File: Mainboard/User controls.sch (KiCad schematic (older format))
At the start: 7 parts, among them J2 JST-PH 01x10, J5 JST-PH 01x02, J6 JST-PH 01x02

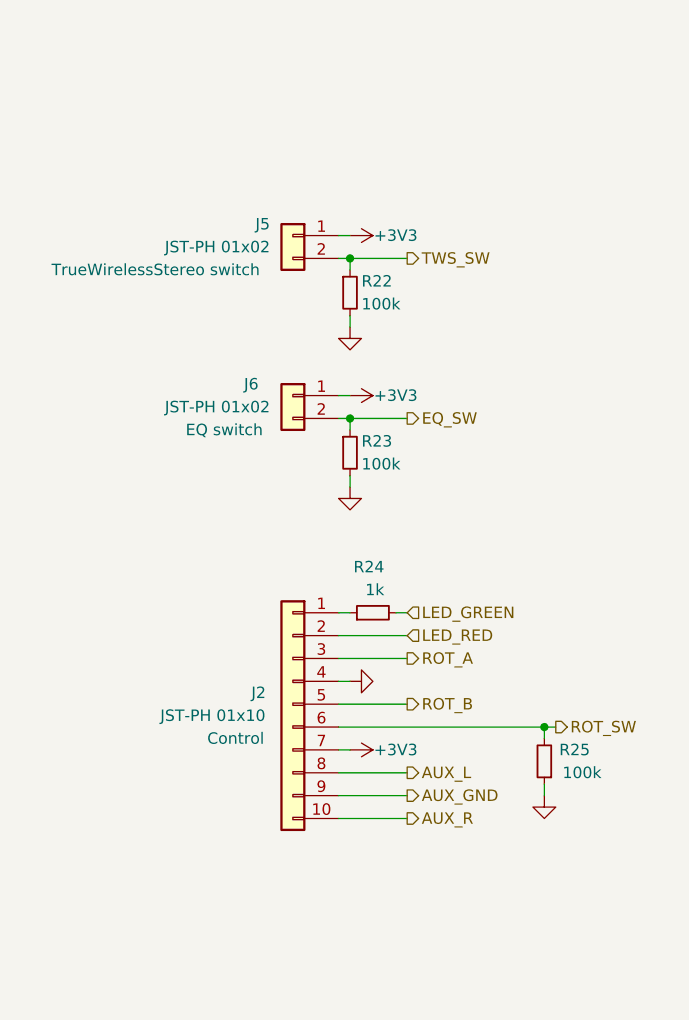
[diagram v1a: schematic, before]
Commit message: Before testing CH340B and VCHG
Cleaned up amp lay-out a bit in the meanwhile
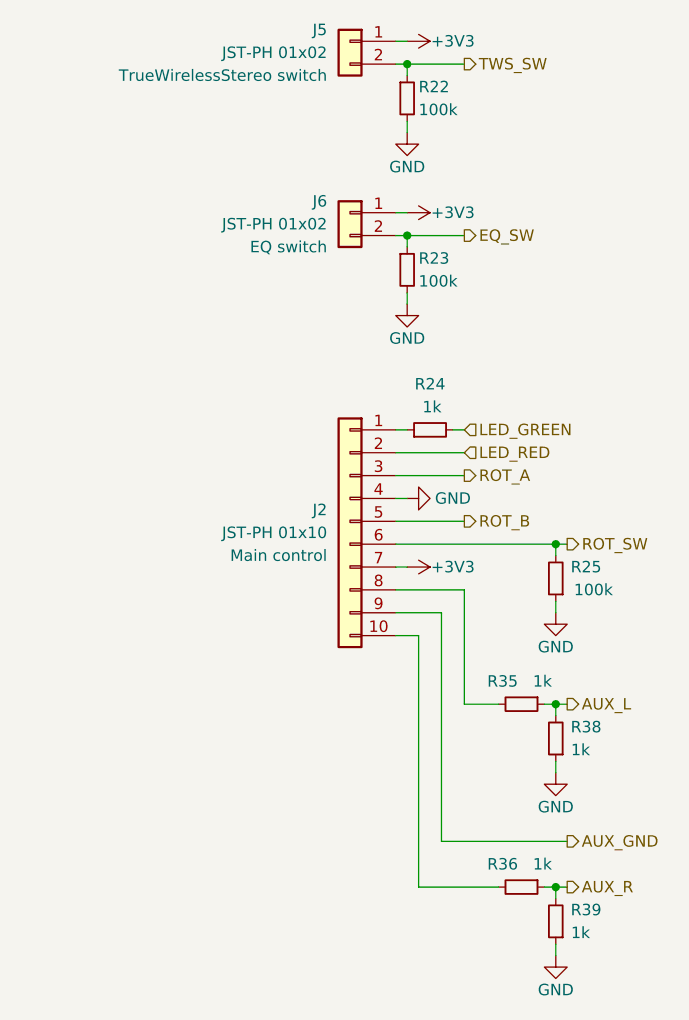
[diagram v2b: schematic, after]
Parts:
- added R35, R36, R38, R39: 1k, Resistor_SMD:R_0603_1608Metric, symbol Device:R_Small
- J2: Function Control -> Main control
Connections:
- net AUX_L: now also R35.1, R38.2; no longer J2.8 (Pin_8)
- net AUX_R: now also R36.1, R39.2; no longer J2.10 (Pin_10)
- net GND: now also R38.1, R39.1
- new net: J2.10 (Pin_10), R36.2
- new net: J2.8 (Pin_8), R35.2
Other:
- moved on the sheet: J2, J5, J6, R22, R23, R24, R25
